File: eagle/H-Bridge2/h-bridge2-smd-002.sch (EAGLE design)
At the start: 36 parts

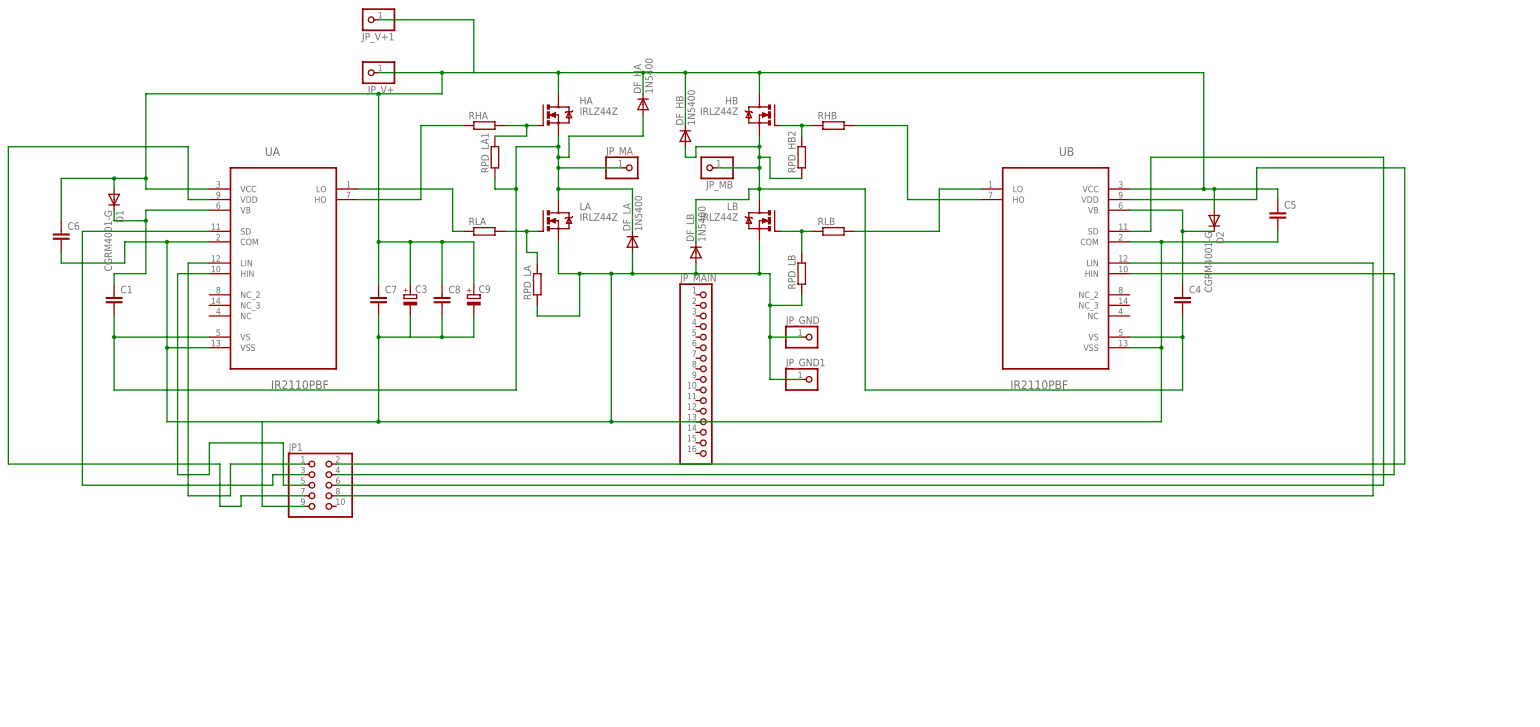
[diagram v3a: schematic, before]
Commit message: SMD for logic drv
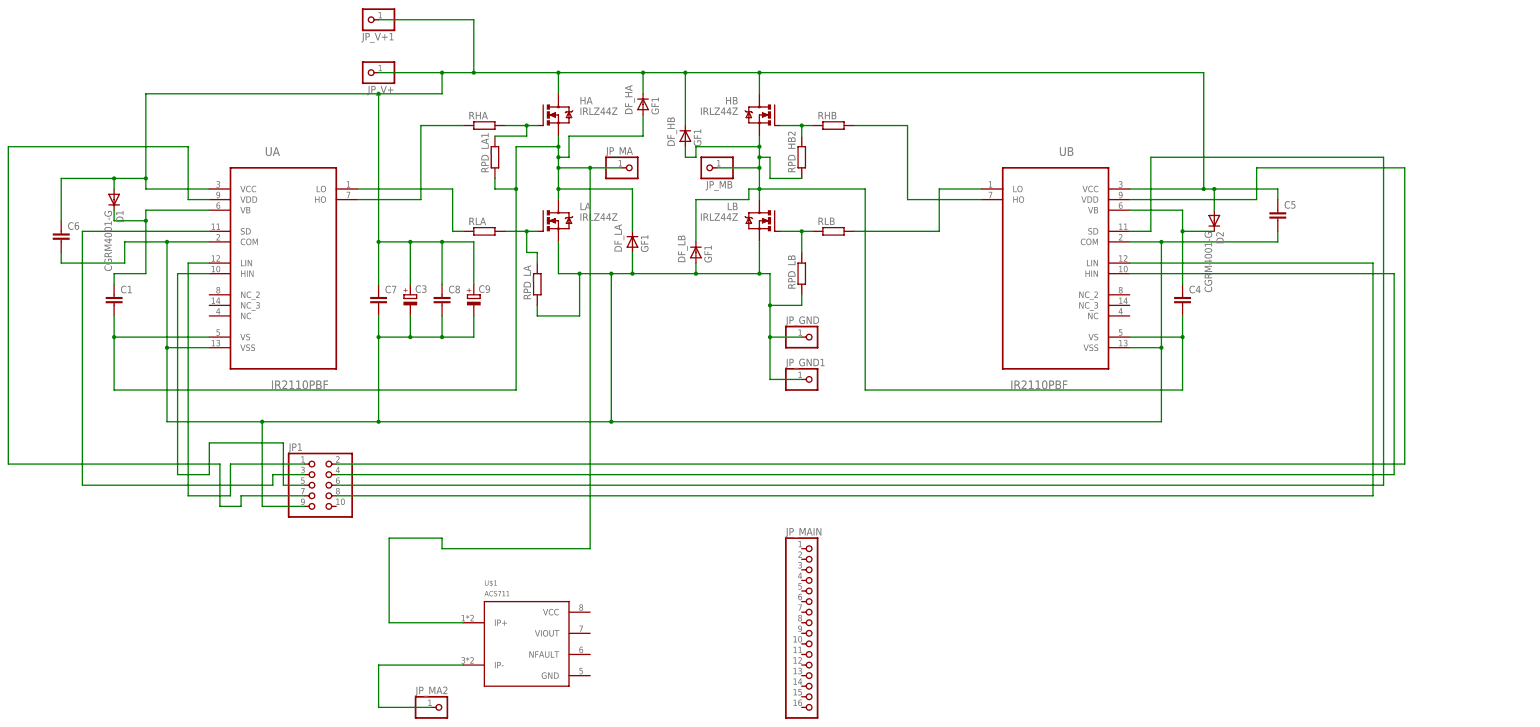
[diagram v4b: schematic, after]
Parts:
- added JP_MA2: (no value), dbg-misc:PINHD-1X1
- added U$1: ACS711, acs711:ACS711
- DF_HA, DF_HB, DF_LA, DF_LB: value 1N5400 -> GF1; device dbg-misc:1N5400 -> diode:GF1
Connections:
- new net N$1: JP_MA2.1, U$1.IP-
- net N$17: now also U$1.IP+
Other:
- moved on the sheet: JP_MAIN
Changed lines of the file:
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@@
 <part name="C5" library="rcl" deviceset="C-EU" device="C4532"/>
 <part name="C6" library="rcl" deviceset="C-EU" device="C4532"/>
-<part name="DF_HA" library="dbg-misc" deviceset="1N5400" device=""/>
-<part name="DF_HB" library="dbg-misc" deviceset="1N5400" device=""/>
-<part name="DF_LB" library="dbg-misc" deviceset="1N5400" device=""/>
-<part name="DF_LA" library="dbg-misc" deviceset="1N5400" device=""/>
+<part name="DF_HA" library="diode" deviceset="GF1" device=""/>
+<part name="DF_HB" library="diode" deviceset="GF1" device=""/>
+<part name="DF_LB" library="diode" deviceset="GF1" device=""/>
+<part name="DF_LA" library="diode" deviceset="GF1" device=""/>
 <part name="C3" library="rcl" deviceset="CPOL-EU" device="E5-13"/>
 <part name="RPD_LB" library="rcl" deviceset="R-EU_" device="R1206"/>
@@
 <part name="JP_V+1" library="dbg-misc" deviceset="PINHD-1X1" device=""/>
 <part name="JP_GND1" library="dbg-misc" deviceset="PINHD-1X1" device=""/>
+<part name="U$1" library="acs711" deviceset="ACS711" device=""/>
+<part name="JP_MA2" library="dbg-misc" deviceset="PINHD-1X1" device=""/>
 </parts>
 <sheets>
@@
 </plain>
 <instances>
-<instance part="JP_MAIN" gate="A" x="12.7" y="50.8"/>
+<instance part="JP_MAIN" gate="A" x="38.1" y="-10.16"/>
 <instance part="HA" gate="G$1" x="-25.4" y="111.76"/>
 <instance part="LA" gate="G$1" x="-25.4" y="86.36"/>
@@
 <instance part="C5" gate="G$1" x="149.86" y="88.9"/>
 <instance part="C6" gate="G$1" x="-142.24" y="83.82"/>
-<instance part="DF_HA" gate="1" x="-2.54" y="114.3" rot="R90"/>
-<instance part="DF_HB" gate="1" x="7.62" y="106.68" rot="R90"/>
-<instance part="DF_LB" gate="1" x="10.16" y="78.74" rot="R90"/>
-<instance part="DF_LA" gate="1" x="-5.08" y="81.28" rot="R90"/>
+<instance part="DF_HA" gate="D" x="-2.54" y="114.3" rot="R90"/>
+<instance part="DF_HB" gate="D" x="7.62" y="106.68" rot="R90"/>
+<instance part="DF_LB" gate="D" x="10.16" y="78.74" rot="R90"/>
+<instance part="DF_LA" gate="D" x="-5.08" y="81.28" rot="R90"/>
 <instance part="C3" gate="G$1" x="-58.42" y="68.58"/>
 <instance part="RPD_LB" gate="G$1" x="35.56" y="73.66" rot="R90"/>
@@
 <instance part="JP_V+1" gate="G$1" x="-68.58" y="134.62" rot="R180"/>
 <instance part="JP_GND1" gate="G$1" x="38.1" y="48.26"/>
+<instance part="U$1" gate="G$1" x="-30.48" y="-15.24"/>
+<instance part="JP_MA2" gate="G$1" x="-50.8" y="-30.48"/>
 </instances>
 <busses>
@@
 <wire x1="-127" y1="81.28" x2="-116.84" y2="81.28" width="0.1524" layer="91"/>
 <junction x="-116.84" y="81.28"/>
-<pinref part="DF_LA" gate="1" pin="A"/>
+<pinref part="DF_LA" gate="D" pin="A"/>
 <wire x1="-5.08" y1="78.74" x2="-5.08" y2="73.66" width="0.1524" layer="91"/>
-<pinref part="DF_LB" gate="1" pin="A"/>
+<pinref part="DF_LB" gate="D" pin="A"/>
 <wire x1="10.16" y1="76.2" x2="10.16" y2="73.66" width="0.1524" layer="91"/>
 <junction x="10.16" y="73.66"/>
@@
 <wire x1="27.94" y1="48.26" x2="27.94" y2="58.42" width="0.1524" layer="91"/>
 <junction x="27.94" y="58.42"/>
+<junction x="-58.42" y="58.42"/>
+<junction x="-93.98" y="38.1"/>
 </segment>
 </net>
@@
 <wire x1="-22.86" y1="99.06" x2="-22.86" y2="93.98" width="0.1524" layer="91"/>
 <wire x1="-22.86" y1="93.98" x2="-22.86" y2="91.44" width="0.1524" layer="91"/>
-<wire x1="-7.62" y1="99.06" x2="-22.86" y2="99.06" width="0.1524" layer="91"/>
+<wire x1="-7.62" y1="99.06" x2="-15.24" y2="99.06" width="0.1524" layer="91"/>
 <junction x="-22.86" y="99.06"/>
+<wire x1="-15.24" y1="99.06" x2="-22.86" y2="99.06" width="0.1524" layer="91"/>
 <wire x1="-33.02" y1="104.14" x2="-22.86" y2="104.14" width="0.1524" layer="91"/>
 <junction x="-129.54" y="58.42"/>
 <junction x="-22.86" y="104.14"/>
-<pinref part="DF_HA" gate="1" pin="A"/>
+<pinref part="DF_HA" gate="D" pin="A"/>
 <wire x1="-2.54" y1="111.76" x2="-2.54" y2="106.68" width="0.1524" layer="91"/>
 <wire x1="-2.54" y1="106.68" x2="-20.32" y2="106.68" width="0.1524" layer="91"/>
@@
 <wire x1="-20.32" y1="101.6" x2="-22.86" y2="101.6" width="0.1524" layer="91"/>
 <junction x="-22.86" y="101.6"/>
-<pinref part="DF_LA" gate="1" pin="C"/>
+<pinref part="DF_LA" gate="D" pin="C"/>
 <wire x1="-5.08" y1="83.82" x2="-5.08" y2="93.98" width="0.1524" layer="91"/>
 <wire x1="-5.08" y1="93.98" x2="-22.86" y2="93.98" width="0.1524" layer="91"/>
@@
 <wire x1="-38.1" y1="93.98" x2="-33.02" y2="93.98" width="0.1524" layer="91"/>
 <junction x="-33.02" y="93.98"/>
+<wire x1="-15.24" y1="99.06" x2="-15.24" y2="7.62" width="0.1524" layer="91"/>
+<wire x1="-15.24" y1="7.62" x2="-50.8" y2="7.62" width="0.1524" layer="91"/>
+<wire x1="-50.8" y1="7.62" x2="-50.8" y2="10.16" width="0.1524" layer="91"/>
+<wire x1="-50.8" y1="10.16" x2="-63.5" y2="10.16" width="0.1524" layer="91"/>
+<wire x1="-63.5" y1="10.16" x2="-63.5" y2="-10.16" width="0.1524" layer="91"/>
+<pinref part="U$1" gate="G$1" pin="IP+"/>
+<wire x1="-63.5" y1="-10.16" x2="-45.72" y2="-10.16" width="0.1524" layer="91"/>
+<junction x="-15.24" y="99.06"/>
 </segment>
 </net>
@@
 <junction x="25.4" y="93.98"/>
 <junction x="127" y="58.42"/>
-<pinref part="DF_HB" gate="1" pin="A"/>
+<pinref part="DF_HB" gate="D" pin="A"/>
 <wire x1="7.62" y1="104.14" x2="7.62" y2="101.6" width="0.1524" layer="91"/>
 <wire x1="7.62" y1="101.6" x2="10.16" y2="101.6" width="0.1524" layer="91"/>
@@
 <wire x1="10.16" y1="104.14" x2="25.4" y2="104.14" width="0.1524" layer="91"/>
 <junction x="25.4" y="104.14"/>
-<pinref part="DF_LB" gate="1" pin="C"/>
+<pinref part="DF_LB" gate="D" pin="C"/>
 <wire x1="10.16" y1="81.28" x2="10.16" y2="91.44" width="0.1524" layer="91"/>
 <wire x1="10.16" y1="91.44" x2="22.86" y2="91.44" width="0.1524" layer="91"/>
@@
 <junction x="-129.54" y="96.52"/>
 <junction x="-22.86" y="121.92"/>
-<pinref part="DF_HA" gate="1" pin="C"/>
+<pinref part="DF_HA" gate="D" pin="C"/>
 <wire x1="-2.54" y1="116.84" x2="-2.54" y2="121.92" width="0.1524" layer="91"/>
-<pinref part="DF_HB" gate="1" pin="C"/>
+<pinref part="DF_HB" gate="D" pin="C"/>
 <wire x1="7.62" y1="109.22" x2="7.62" y2="121.92" width="0.1524" layer="91"/>
 <junction x="-2.54" y="121.92"/>
@@
 <wire x1="-66.04" y1="134.62" x2="-43.18" y2="134.62" width="0.1524" layer="91"/>
 <wire x1="-43.18" y1="134.62" x2="-43.18" y2="121.92" width="0.1524" layer="91"/>
+<junction x="-43.18" y="121.92"/>
 </segment>
 </net>
@@
 </segment>
 </net>
+<net name="N$1" class="0">
+<segment>
+<pinref part="U$1" gate="G$1" pin="IP-"/>
+<wire x1="-45.72" y1="-20.32" x2="-66.04" y2="-20.32" width="0.1524" layer="91"/>
+<wire x1="-66.04" y1="-20.32" x2="-66.04" y2="-30.48" width="0.1524" layer="91"/>
+<pinref part="JP_MA2" gate="G$1" pin="1"/>
+<wire x1="-66.04" y1="-30.48" x2="-53.34" y2="-30.48" width="0.1524" layer="91"/>
+</segment>
+</net>
